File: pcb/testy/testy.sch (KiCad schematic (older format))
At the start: 70 parts, among them P1 OLED, P2 ICSP, SW0:0 SW_Push, SW0:1 SW_Push, SW0:2 SW_Push, SW0:3 SW_Push, SW0:4 SW_Push, SW1:0 SW_Push, SW1:1 SW_Push, SW1:2 SW_Push, SW1:3 SW_Push, SW1:4 SW_Push, SW2:0 SW_Push, SW2:1 SW_Push, SW2:2 SW_Push, SW2:3 SW_Push, SW2:4 SW_Push, SW3:0 SW_Push, SW3:1 SW_Push, SW3:2 SW_Push, SW3:3 SW_Push, SW3:4 SW_Push, SW3:5 SW_Push, SW4:1 SW_Push, SW4:2 SW_Push, SW4:3 SW_Push, SW4:4 SW_Push, SW4:5 SW_Push

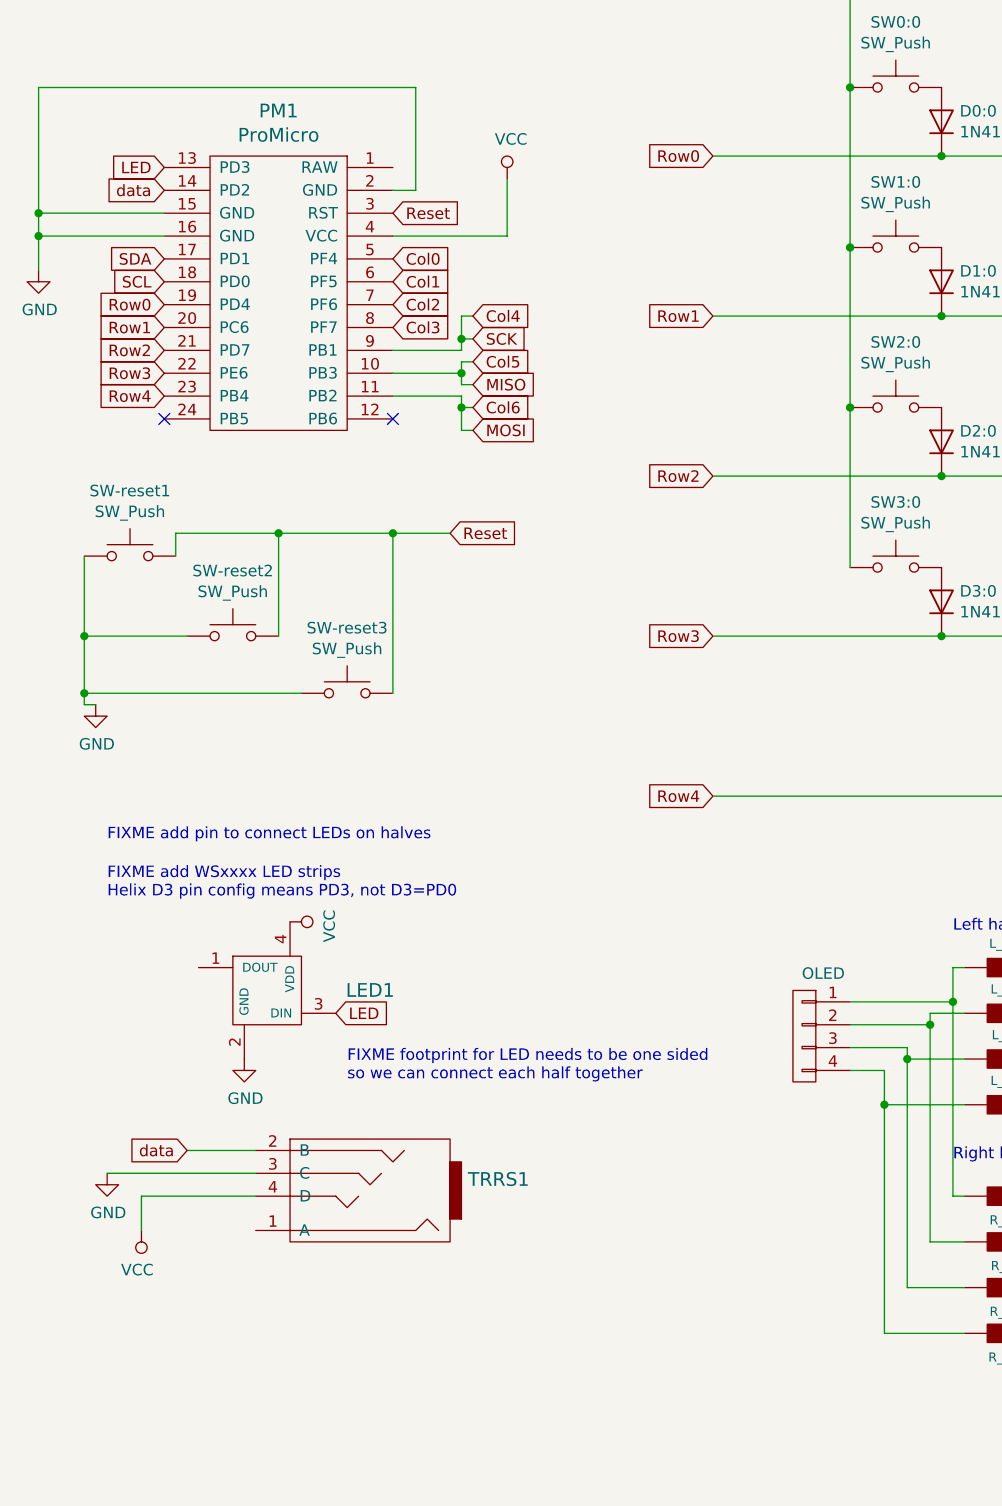
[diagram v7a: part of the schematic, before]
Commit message: fix: correct (I think) the LED wiring
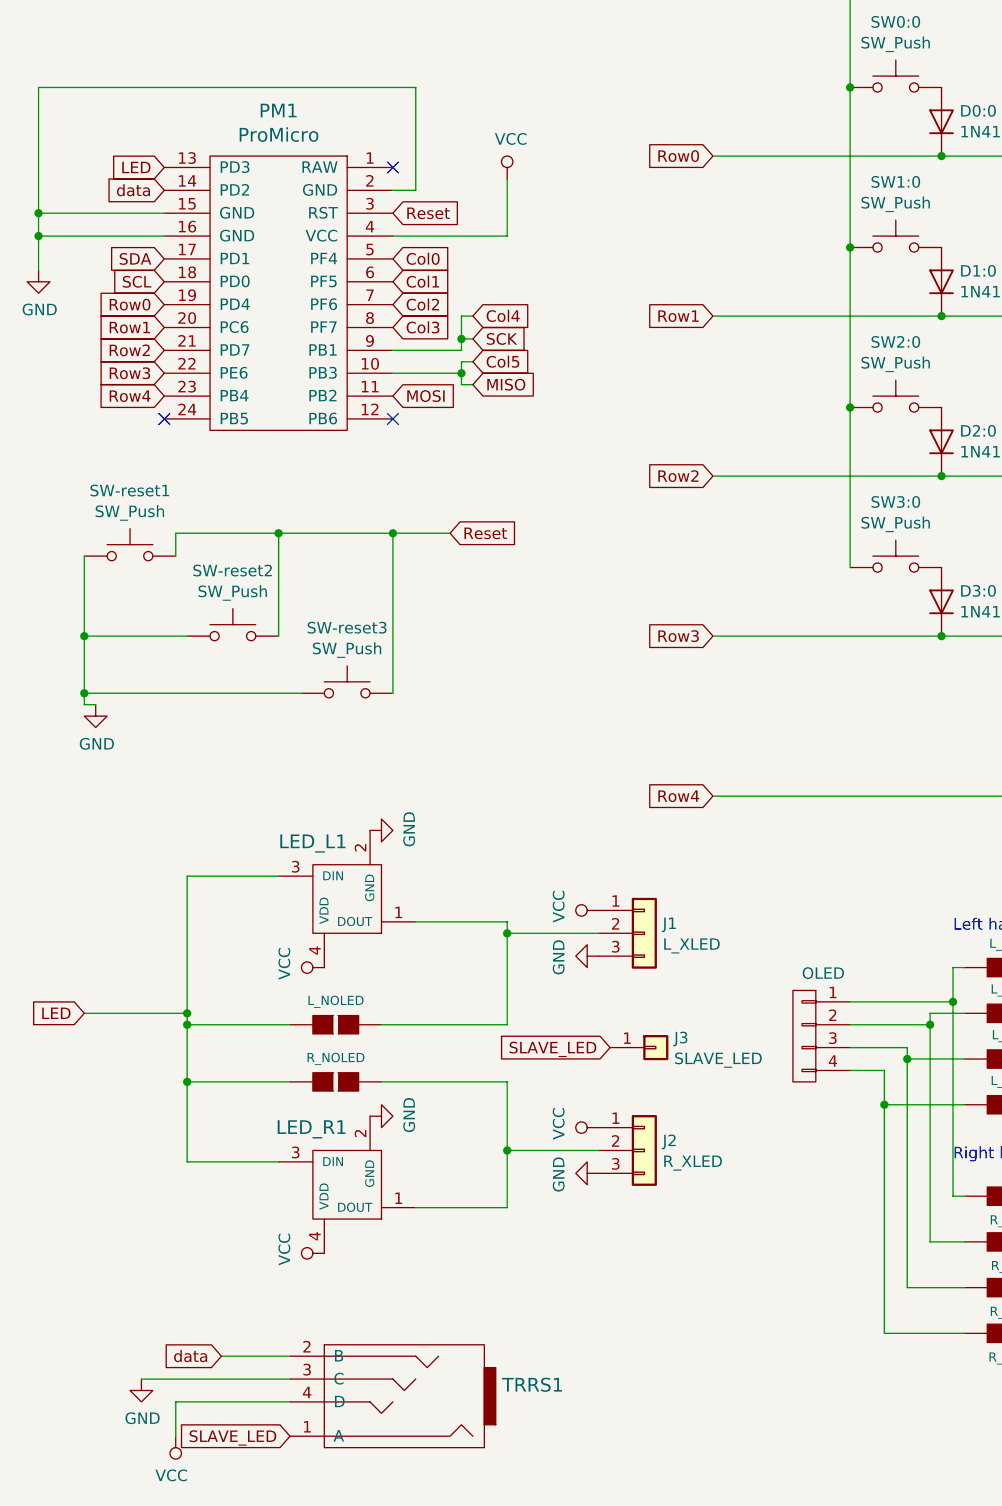
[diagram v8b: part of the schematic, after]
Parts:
- added J1: L_XLED, footprints:ws2812-strip, symbol this_keeb:Conn_01x03
- added J2: R_XLED, footprints:ws2812-strip, symbol this_keeb:Conn_01x03
- added J3: SLAVE_LED, footprints:PinHeader_1x01_P2.54mm_Vertical, symbol this_keeb:Conn_01x01
- added JP12: R_NOLED, footprints:Jumper, symbol jp2:JP2
- added JP9: L_NOLED, footprints:Jumper, symbol jp2:JP2
- added LED_R1: SK6812mini, footprints:ws2812-single, symbol sk6812mini:SK6812mini
- renumbered LED1 to LED_L1
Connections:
- net GND: now also J1.3 (Pin_3), J2.3 (Pin_3), LED_R1.2 (GND)
- net LED: now also JP12.2 (G2), JP9.2 (G2), LED_R1.3 (DIN)
- net VCC: now also J1.1 (Pin_1), J2.1 (Pin_1), LED_R1.4 (VDD)
- net SLAVE_LED: now reaches TRRS1.1 (A)
- net SLAVE_LED: now also J3.1 (Pin_1)
- net at LED_L1.1 (DOUT): now also J1.2 (Pin_2), JP9.1 (G1)
- net Col6 renamed MOSI
- new net: J2.2 (Pin_2), JP12.1 (G1), LED_R1.1 (DOUT)
- no-connect marks 2 -> 3
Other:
- note removed: "FIXME add WSxxxx LED strips\nHelix D3 pin config means PD3, not D3=PD0"
- note removed: "FIXME add pin to connect LEDs on halves"
- note removed: "FIXME footprint for LED needs to be one sided\nso we can connect each half together"
- moved on the sheet: LED_L1, TRRS1
